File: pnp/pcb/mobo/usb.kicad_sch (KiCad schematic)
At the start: 4 parts, among them J9 USB_B, U8 SRV05-4

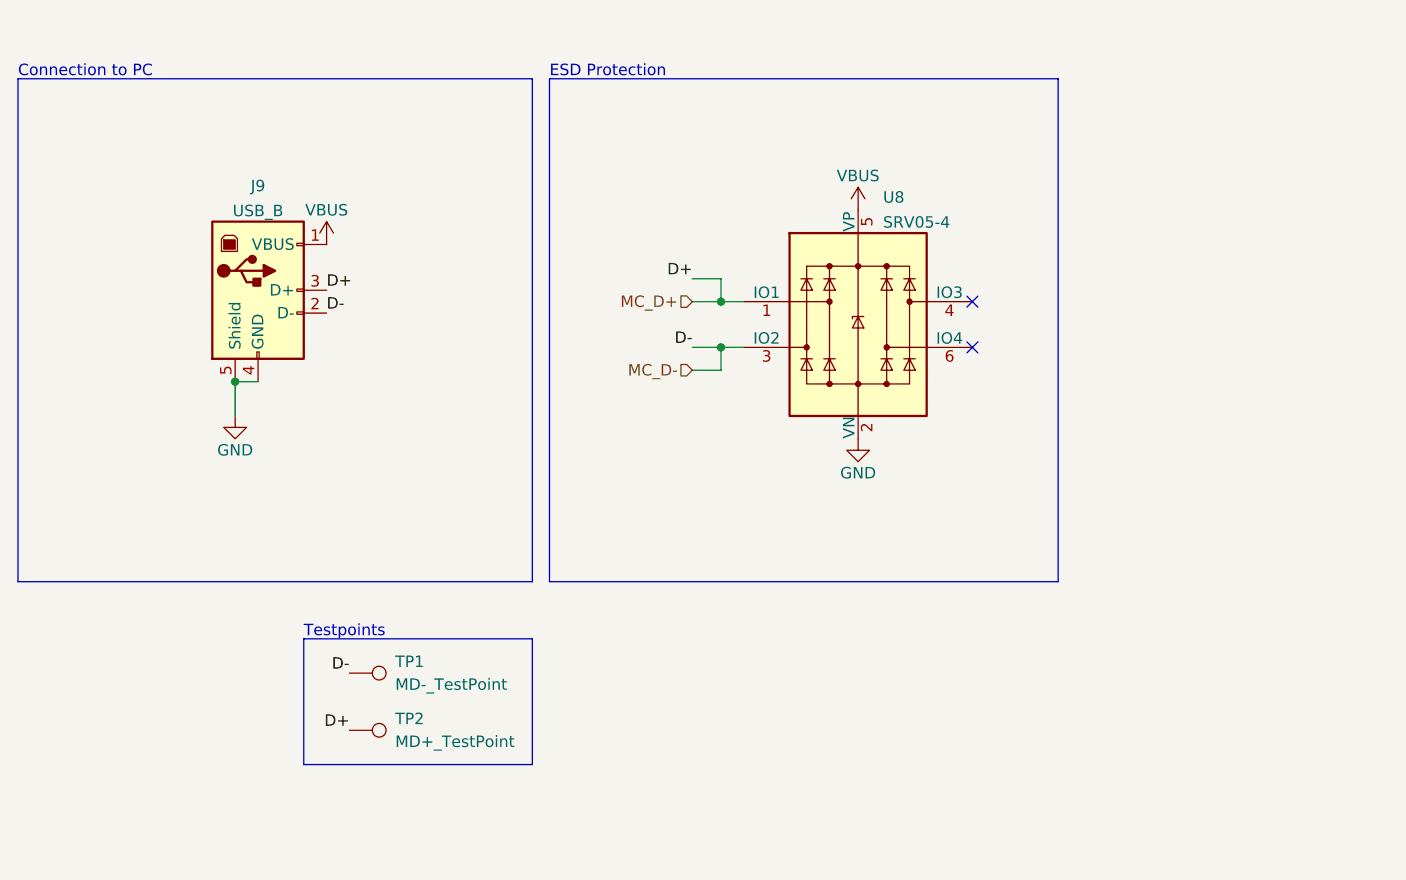
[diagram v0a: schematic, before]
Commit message: Mobo V4A Redesign
Some EMC improvements to schematics.
Reassigned MCU Pins for HW-PWM support.
Changes are still marked with text in the schematics.
Complete PCB Layout reworked
Status: Needs to be verified, and cleaned up a little, but DRC is running green.
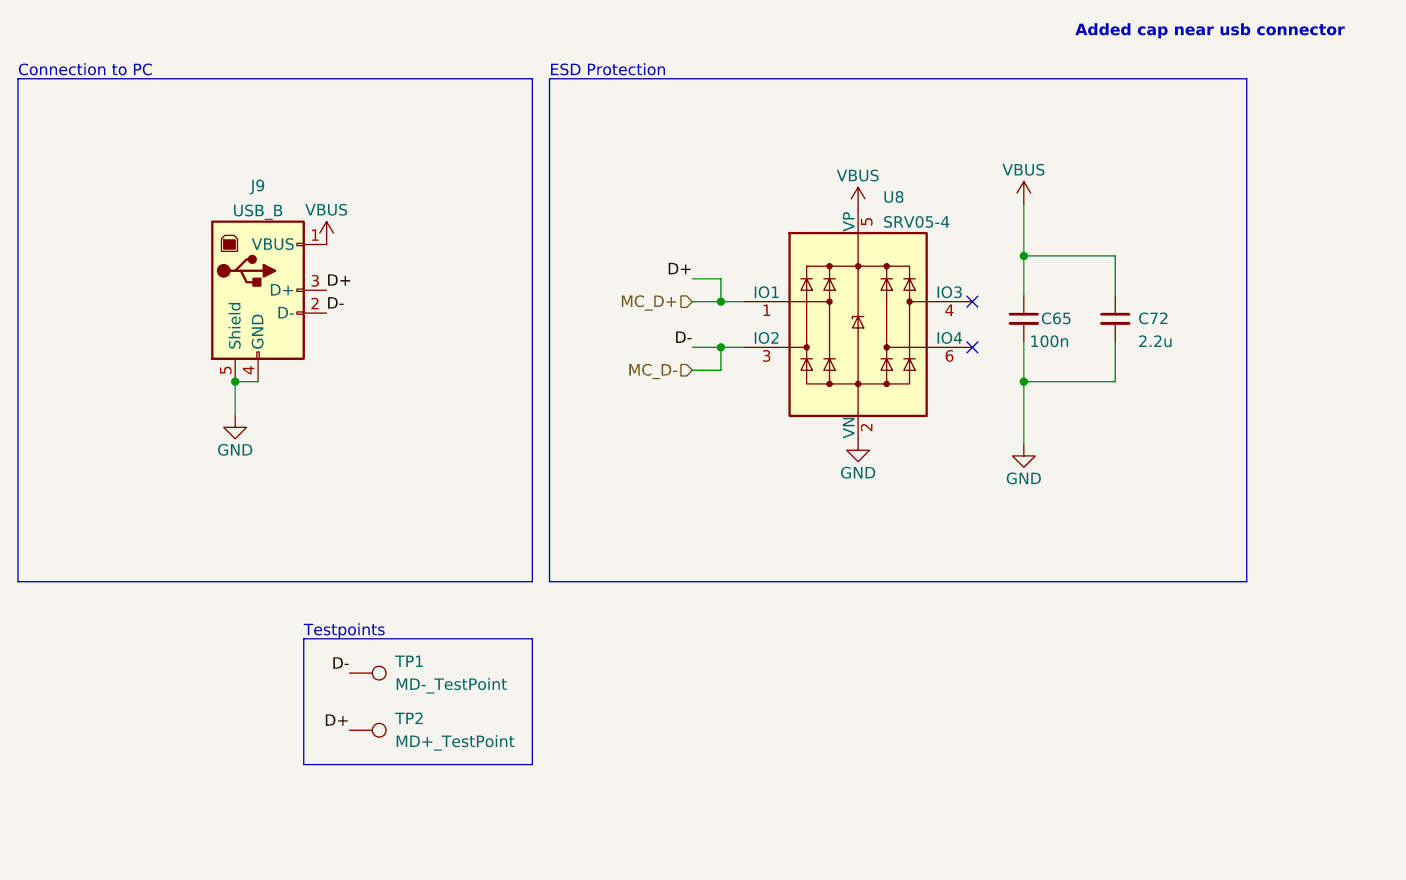
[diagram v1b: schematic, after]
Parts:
- added C65: 100n, Capacitor_SMD:C_0805_2012Metric, symbol Device:C_Small
- added C72: 2.2u, Capacitor_SMD:C_0805_2012Metric, symbol Device:C_Small
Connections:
- net GND: now also C65.2, C72.2
- net VBUS: now also C65.1, C72.1
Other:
- note added: "Added cap near usb connector"
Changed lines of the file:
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@@
   (title_block
     (title "LumenPnP Motherboard")
-    (date "2022-03-29")
-    (rev "003")
+    (date "2022-09-09")
+    (rev "004A")
     (company "Opulo")
+    (comment 1 "Reengineered by Magpie")
   )
   (junction (at 74.93 85.725) (diameter 0) (color 0 0 0 0)
   )
   (junction (at 128.905 76.835) (diameter 0) (color 0 0 0 0)
+  )
+  (junction (at 162.56 85.725) (diameter 0) (color 0 0 0 0)
+  )
+  (junction (at 162.56 71.755) (diameter 0) (color 0 0 0 0)
   )
   (junction (at 128.905 81.915) (diameter 0) (color 0 0 0 0)
@@
   (no_connect (at 156.845 76.835))
   (no_connect (at 156.845 81.915))
+  (wire (pts (xy 162.56 66.04) (xy 162.56 71.755))
+    (stroke (width 0) (type default) (color 0 0 0 0))
+  )
+  (wire (pts (xy 162.56 85.725) (xy 162.56 81.28))
+    (stroke (width 0) (type default) (color 0 0 0 0))
+  )
   (polyline (pts (xy 107.95 52.07) (xy 107.95 107.95))
     (stroke (width 0) (type default) (color 0 0 0 0))
@@
     (stroke (width 0) (type default) (color 0 0 0 0))
   )
+  (wire (pts (xy 162.56 71.755) (xy 172.72 71.755))
+    (stroke (width 0) (type default) (color 0 0 0 0))
+  )
+  (wire (pts (xy 172.72 85.725) (xy 162.56 85.725))
+    (stroke (width 0) (type default) (color 0 0 0 0))
+  )
   (wire (pts (xy 128.905 74.295) (xy 128.905 76.835))
     (stroke (width 0) (type default) (color 0 0 0 0))
   )
+  (wire (pts (xy 162.56 71.755) (xy 162.56 76.2))
+    (stroke (width 0) (type default) (color 0 0 0 0))
+  )
   (wire (pts (xy 128.905 81.915) (xy 131.445 81.915))
     (stroke (width 0) (type default) (color 0 0 0 0))
@@
     (stroke (width 0) (type default) (color 0 0 0 0))
   )
-  (polyline (pts (xy 166.37 107.95) (xy 109.855 107.95))
+  (wire (pts (xy 172.72 81.28) (xy 172.72 85.725))
+    (stroke (width 0) (type default) (color 0 0 0 0))
+  )
+  (polyline (pts (xy 187.325 107.95) (xy 109.855 107.95))
     (stroke (width 0) (type default) (color 0 0 0 0))
   )
@@
     (stroke (width 0) (type default) (color 0 0 0 0))
   )
-  (polyline (pts (xy 109.855 52.07) (xy 166.37 52.07))
-    (stroke (width 0) (type default) (color 0 0 0 0))
-  )
-  (polyline (pts (xy 166.37 52.07) (xy 166.37 107.95))
+  (polyline (pts (xy 109.855 52.07) (xy 187.325 52.07))
+    (stroke (width 0) (type default) (color 0 0 0 0))
+  )
+  (polyline (pts (xy 187.325 52.07) (xy 187.325 107.95))
+    (stroke (width 0) (type default) (color 0 0 0 0))
+  )
+  (wire (pts (xy 162.56 92.71) (xy 162.56 85.725))
+    (stroke (width 0) (type default) (color 0 0 0 0))
+  )
+  (wire (pts (xy 172.72 76.2) (xy 172.72 71.755))
     (stroke (width 0) (type default) (color 0 0 0 0))
   )
@@
   (text "Connection to PC" (at 50.8 52.07 0)
     (effects (font (size 1.27 1.27)) (justify left bottom))
+  )
+  (text "Added cap near usb connector" (at 168.275 47.625 0)
+    (effects (font (size 1.27 1.27) (thickness 0.254) bold) (justify left bottom))
   )
   (label "D-" (at 125.73 81.915 180)
@@
     (pin "1")
   )
+  (symbol (lib_id "power:VBUS") (at 162.56 66.04 0) (unit 1)
+    (in_bom yes) (on_board yes)
+    (property "Reference" "#PWR03" (id 0) (at 162.56 69.85 0)
+      (effects (font (size 1.27 1.27)) hide)
+    )
+    (property "Value" "VBUS" (id 1) (at 162.56 62.23 0))
+    (property "Footprint" "" (id 2) (at 162.56 66.04 0)
+      (effects (font (size 1.27 1.27)) hide)
+    )
+    (property "Datasheet" "" (id 3) (at 162.56 66.04 0)
+      (effects (font (size 1.27 1.27)) hide)
+    )
+    (pin "1")
+  )
   (symbol (lib_id "power:GND") (at 74.93 89.535 0) (mirror y) (unit 1)
     (in_bom yes) (on_board yes)
@@
     )
     (pin "1")
+  )
+  (symbol (lib_id "power:GND") (at 162.56 92.71 0) (mirror y) (unit 1)
+    (in_bom yes) (on_board yes)
+    (property "Reference" "#PWR05" (id 0) (at 162.56 99.06 0)
+      (effects (font (size 1.27 1.27)) hide)
+    )
+    (property "Value" "GND" (id 1) (at 162.56 96.52 0))
+    (property "Footprint" "" (id 2) (at 162.56 92.71 0)
+      (effects (font (size 1.27 1.27)) hide)
+    )
+    (property "Datasheet" "" (id 3) (at 162.56 92.71 0)
+      (effects (font (size 1.27 1.27)) hide)
+    )
+    (pin "1")
+  )
+  (symbol (lib_id "Device:C_Small") (at 162.56 78.74 0) (unit 1)
+    (in_bom yes) (on_board yes)
+    (property "Reference" "C65" (id 0) (at 164.465 78.74 0)
+      (effects (font (size 1.27 1.27)) (justify left))
+    )
+    (property "Value" "100n" (id 1) (at 163.195 81.28 0)
+      (effects (font (size 1.27 1.27)) (justify left))
+    )
+    (property "Footprint" "Capacitor_SMD:C_0805_2012Metric" (id 2) (at 162.56 78.74 0)
+      (effects (font (size 1.27 1.27)) hide)
+    )
+    (property "Datasheet" "" (id 3) (at 162.56 78.74 0)
+      (effects (font (size 1.27 1.27)) hide)
+    )
+    (property "Digikey" "1276-1180-1-ND" (id 4) (at 162.56 78.74 0)
+      (effects (font (size 1.27 1.27)) hide)
+    )
+    (property "JLCPCB" "C49678" (id 5) (at 162.56 78.74 0)
+      (effects (font (size 1.27 1.27)) hide)
+    )
+    (property "LCSC" "C360619" (id 6) (at 162.56 78.74 0)
+      (effects (font (size 1.27 1.27)) hide)
+    )
+    (property "Mouser" "581-08055C104K" (id 7) (at 162.56 78.74 0)
+      (effects (font (size 1.27 1.27)) hide)
+    )
+    (pin "1")
+    (pin "2")
   )
   (symbol (lib_id "Power_Protection:SRV05-4") (at 144.145 79.375 0) (unit 1)
@@
     (pin "5")
   )
+  (symbol (lib_id "Device:C_Small") (at 172.72 78.74 0) (unit 1)
+    (in_bom yes) (on_board yes)
+    (property "Reference" "C72" (id 0) (at 175.26 78.74 0)
+      (effects (font (size 1.27 1.27)) (justify left))
+    )
+    (property "Value" "2.2u" (id 1) (at 175.26 81.28 0)
+      (effects (font (size 1.27 1.27)) (justify left))
+    )
+    (property "Footprint" "Capacitor_SMD:C_0805_2012Metric" (id 2) (at 172.72 78.74 0)
+      (effects (font (size 1.27 1.27)) hide)
+    )
+    (property "Datasheet" "" (id 3) (at 172.72 78.74 0)
+      (effects (font (size 1.27 1.27)) hide)
+    )
+    (property "Digikey" "587-4961-1-ND" (id 4) (at 172.72 78.74 0)
+      (effects (font (size 1.27 1.27)) hide)
+    )
+    (property "JLCPCB" "C49217" (id 5) (at 172.72 78.74 0)
+      (effects (font (size 1.27 1.27)) hide)
+    )
+    (property "LCSC" "C49217" (id 6) (at 172.72 78.74 0)
+      (effects (font (size 1.27 1.27)) hide)
+    )
+    (property "Mouser" "963-UMK212ABJ225KG-T" (id 7) (at 172.72 78.74 0)
+      (effects (font (size 1.27 1.27)) hide)
+    )
+    (pin "1")
+    (pin "2")
+  )
   (symbol (lib_id "power:VBUS") (at 144.145 66.675 0) (unit 1)

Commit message: Redesign finished
Completed Board redesign and adding more EMC improvements.
Changed all the part numbers to have a Mouser orderable design (except the JST connectors)
All outputs generated
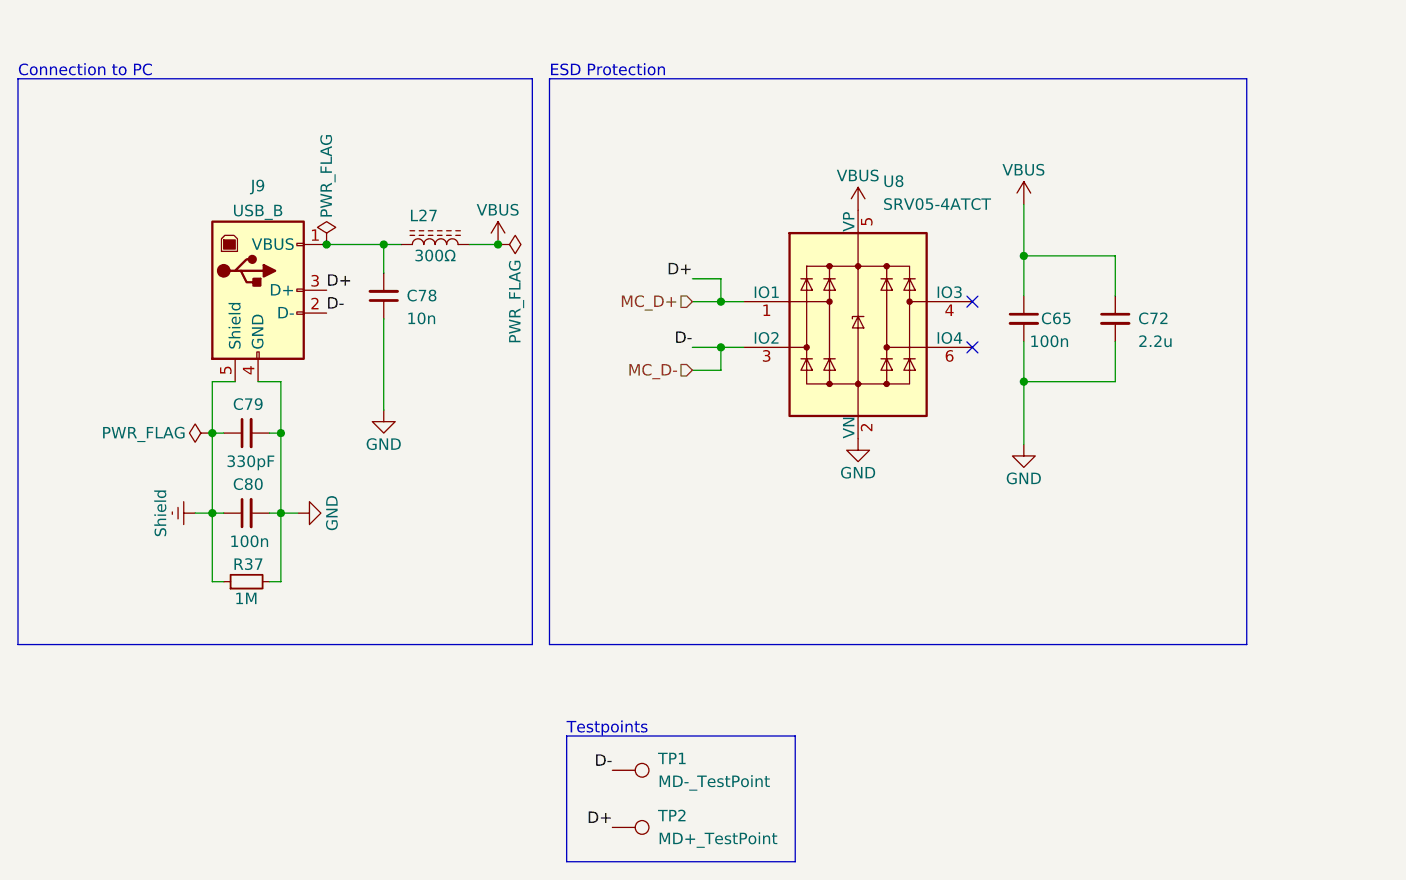
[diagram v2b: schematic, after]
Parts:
- added C78: 10n, Capacitor_SMD:C_0805_2012Metric, symbol Device:C_Small
- added C79: 330pF, Capacitor_SMD:C_0805_2012Metric, symbol Device:C_Small
- added C80: 100n, Capacitor_SMD:C_0805_2012Metric, symbol Device:C_Small
- added L27: 300Ω, Inductor_SMD:L_0805_2012Metric, symbol Device:300Ω
- added R37: 1M, Resistor_SMD:R_0805_2012Metric, symbol Device:R_Small
- C65: Digikey 1276-1180-1-ND -> (none); JLCPCB C49678 -> (none); LCSC C360619 -> (none); Mouser 581-08055C104K -> 710-885012207098
- C72: Digikey 587-4961-1-ND -> (none); JLCPCB C49217 -> (none); LCSC C49217 -> (none); Mouser 963-UMK212ABJ225KG-T -> 810-C2012X5R1H225K
- J9: Mouser (none) -> 710-61400416121
- TP1, TP2: Mouser (none) -> -
- U8: value SRV05-4 -> SRV05-4ATCT; Mouser (none) -> 947-SRV05-4ATCT
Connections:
- net GND: now also C78.1, C79.2, C80.2, R37.2; no longer J9.5 (Shield)
- net VBUS: now also L27.2; no longer J9.1 (VBUS)
- new net Earth: C79.1, C80.1, J9.5 (Shield), R37.1
- new net pwr: C78.2, J9.1 (VBUS), L27.1
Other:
- note removed: "Added cap near usb connector"
- company: Opulo -> Opulo.io
- moved on the sheet: TP1, TP2
